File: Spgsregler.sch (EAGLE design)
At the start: 13 parts, among them X4 22-23-2031, X5 22-23-2031

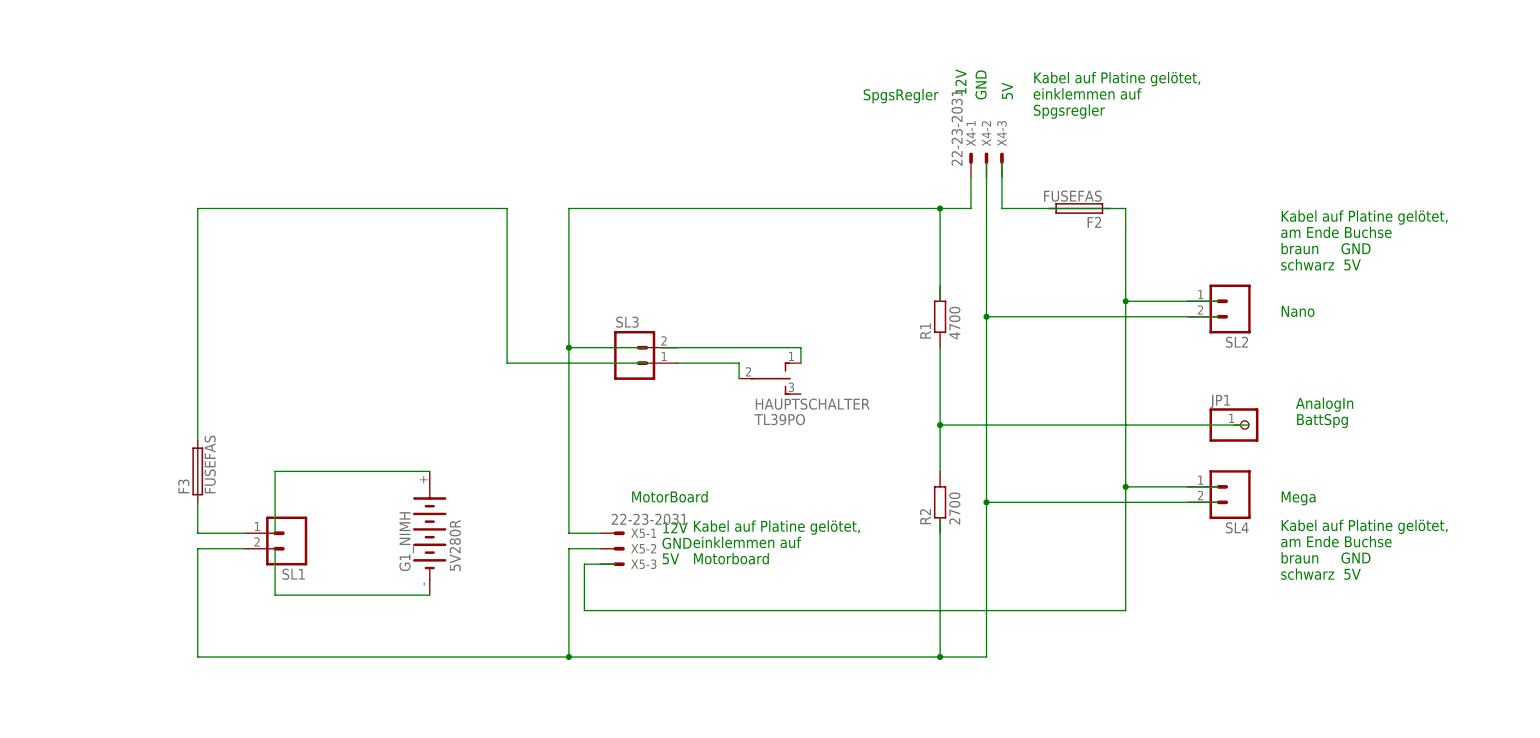
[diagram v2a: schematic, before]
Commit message: 
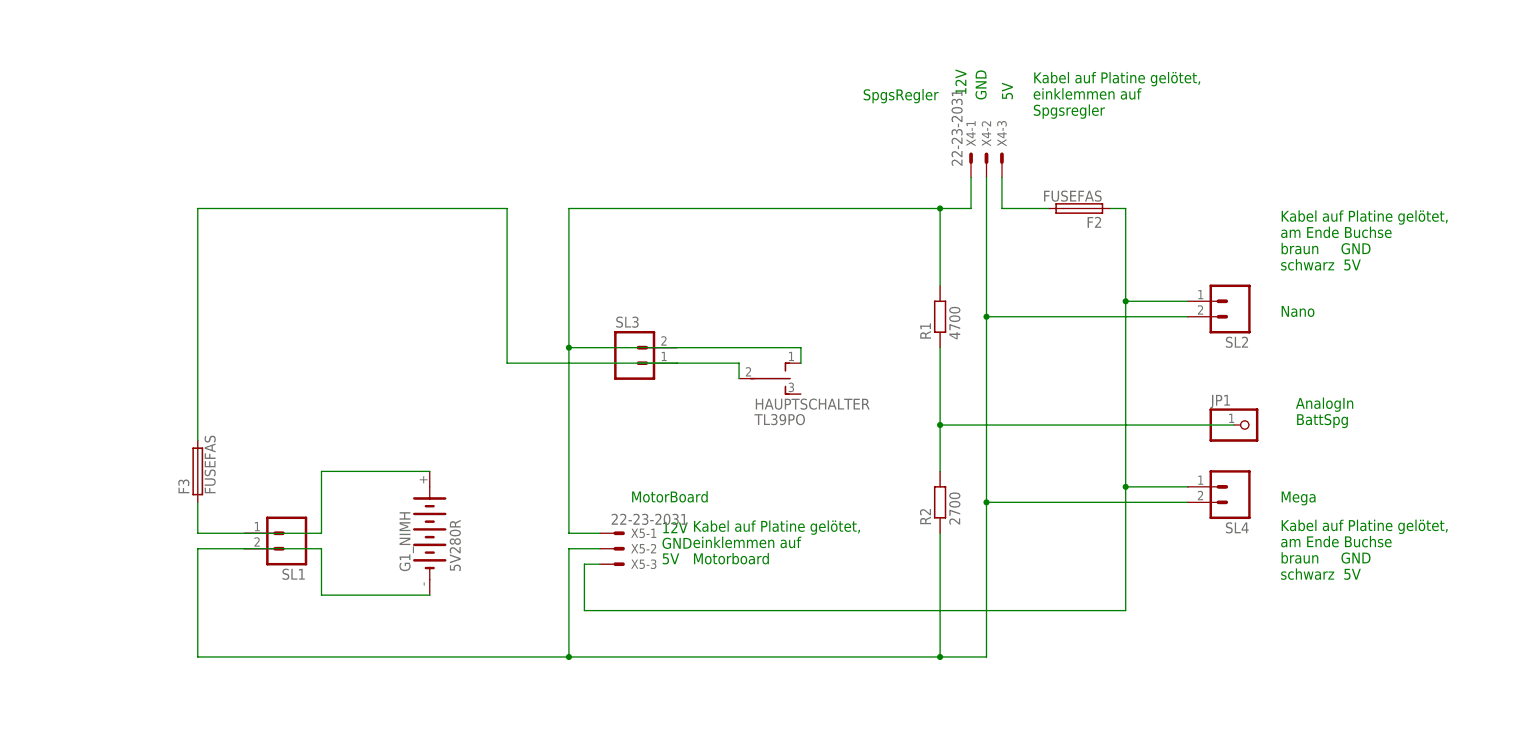
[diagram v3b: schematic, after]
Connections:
- removed net N$1: G1_NIMH.+
- removed net N$10: HAUPTSCHALTER.O
- removed net N$11: SL1.2, X5-2.S
- removed net N$9: HAUPTSCHALTER.P, SL3.1
- new net N$6: F2.2, X4-3.S
- net N$12: now also SL2.1, SL4.1, X5-3.S; no longer F2.2
- net N$2: now also R2.1, SL1.2, SL2.2, SL4.2, X4-2.S, X5-2.S
- net N$3: now also JP1.1
- net N$4: now also G1_NIMH.+; no longer SL1.1
- net N$5: now also HAUPTSCHALTER.O, R1.2
- net N$8: now also HAUPTSCHALTER.P, SL3.1
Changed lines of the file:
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@@
 <part name="X4" library="con-molex" deviceset="22-23-2031" device=""/>
 <part name="X5" library="con-molex" deviceset="22-23-2031" device=""/>
-<part name="FRAME1" library="frames" deviceset="A4L-LOC" device=""/>
+<part name="FRAME1" library="frames" deviceset="A4L-LOC" device="" value="WERTWERT"/>
 <part name="SL2" library="con-amp-quick" deviceset="M02" device=""/>
 <part name="SL4" library="con-amp-quick" deviceset="M02" device=""/>
@@
 </busses>
 <nets>
-<net name="N$1" class="0">
-<segment>
-<pinref part="G1_NIMH" gate="G$1" pin="+"/>
-<wire x1="43.18" y1="35.56" x2="17.78" y2="35.56" width="0.1524" layer="91"/>
-<wire x1="17.78" y1="35.56" x2="17.78" y2="25.4" width="0.1524" layer="91"/>
-</segment>
-</net>
-<net name="N$2" class="0">
-<segment>
-<wire x1="17.78" y1="22.86" x2="17.78" y2="15.24" width="0.1524" layer="91"/>
-<pinref part="G1_NIMH" gate="G$1" pin="-"/>
-<wire x1="17.78" y1="15.24" x2="43.18" y2="15.24" width="0.1524" layer="91"/>
-</segment>
-</net>
 <net name="N$8" class="0">
 <segment>
 <pinref part="F3" gate="G$1" pin="2"/>
-<wire x1="78.74" y1="53.34" x2="55.88" y2="53.34" width="0.1524" layer="91"/>
+<wire x1="83.82" y1="53.34" x2="55.88" y2="53.34" width="0.1524" layer="91"/>
 <wire x1="55.88" y1="78.74" x2="55.88" y2="53.34" width="0.1524" layer="91"/>
 <wire x1="5.08" y1="78.74" x2="55.88" y2="78.74" width="0.1524" layer="91"/>
 <wire x1="5.08" y1="40.64" x2="5.08" y2="78.74" width="0.1524" layer="91"/>
-</segment>
-</net>
-<net name="N$9" class="0">
-<segment>
 <pinref part="SL3" gate="G$1" pin="1"/>
 <pinref part="HAUPTSCHALTER" gate="BEF1" pin="P"/>
@@
 </segment>
 </net>
-<net name="N$10" class="0">
-<segment>
-<pinref part="HAUPTSCHALTER" gate="BEF1" pin="O"/>
-<wire x1="104.14" y1="53.34" x2="104.14" y2="55.88" width="0.1524" layer="91"/>
-<wire x1="104.14" y1="55.88" x2="81.28" y2="55.88" width="0.1524" layer="91"/>
-</segment>
-</net>
 <net name="N$12" class="0">
 <segment>
-<wire x1="144.78" y1="78.74" x2="154.94" y2="78.74" width="0.1524" layer="91"/>
-<pinref part="F2" gate="G$1" pin="2"/>
-<pinref part="F2" gate="G$1" pin="1"/>
-<wire x1="137.16" y1="86.36" x2="137.16" y2="78.74" width="0.1524" layer="91"/>
-<wire x1="137.16" y1="78.74" x2="144.78" y2="78.74" width="0.1524" layer="91"/>
-<wire x1="154.94" y1="78.74" x2="157.48" y2="78.74" width="0.1524" layer="91"/>
 <wire x1="157.48" y1="78.74" x2="157.48" y2="63.5" width="0.1524" layer="91"/>
 <wire x1="157.48" y1="63.5" x2="157.48" y2="33.02" width="0.1524" layer="91"/>
@@
 <wire x1="157.48" y1="12.7" x2="68.58" y2="12.7" width="0.1524" layer="91"/>
 <wire x1="68.58" y1="12.7" x2="68.58" y2="20.32" width="0.1524" layer="91"/>
-<wire x1="68.58" y1="20.32" x2="73.66" y2="20.32" width="0.1524" layer="91"/>
-<wire x1="172.72" y1="63.5" x2="157.48" y2="63.5" width="0.1524" layer="91"/>
-<wire x1="172.72" y1="33.02" x2="157.48" y2="33.02" width="0.1524" layer="91"/>
+<pinref part="F2" gate="G$1" pin="1"/>
+<wire x1="154.94" y1="78.74" x2="157.48" y2="78.74" width="0.1524" layer="91"/>
+<pinref part="SL2" gate="G$1" pin="1"/>
+<wire x1="167.64" y1="63.5" x2="157.48" y2="63.5" width="0.1524" layer="91"/>
 <junction x="157.48" y="63.5"/>
+<pinref part="SL4" gate="G$1" pin="1"/>
+<wire x1="167.64" y1="33.02" x2="157.48" y2="33.02" width="0.1524" layer="91"/>
 <junction x="157.48" y="33.02"/>
+<pinref part="X5" gate="-3" pin="S"/>
+<wire x1="68.58" y1="20.32" x2="71.12" y2="20.32" width="0.1524" layer="91"/>
 </segment>
 </net>
 <net name="N$4" class="0">
 <segment>
-<pinref part="SL1" gate="G$1" pin="1"/>
-<wire x1="12.7" y1="25.4" x2="5.08" y2="25.4" width="0.1524" layer="91"/>
+<pinref part="G1_NIMH" gate="G$1" pin="+"/>
+<wire x1="43.18" y1="35.56" x2="25.4" y2="35.56" width="0.1524" layer="91"/>
+<wire x1="25.4" y1="35.56" x2="25.4" y2="25.4" width="0.1524" layer="91"/>
 <pinref part="F3" gate="G$1" pin="1"/>
 <wire x1="5.08" y1="30.48" x2="5.08" y2="25.4" width="0.1524" layer="91"/>
+<wire x1="25.4" y1="25.4" x2="5.08" y2="25.4" width="0.1524" layer="91"/>
 </segment>
 </net>
 <net name="N$5" class="0">
 <segment>
-<wire x1="78.74" y1="55.88" x2="66.04" y2="55.88" width="0.1524" layer="91"/>
 <wire x1="66.04" y1="55.88" x2="66.04" y2="78.74" width="0.1524" layer="91"/>
 <wire x1="66.04" y1="78.74" x2="127" y2="78.74" width="0.1524" layer="91"/>
@@
 <pinref part="X4" gate="-1" pin="S"/>
 <wire x1="132.08" y1="78.74" x2="132.08" y2="83.82" width="0.1524" layer="91"/>
-<wire x1="127" y1="63.5" x2="127" y2="78.74" width="0.1524" layer="91"/>
+<pinref part="HAUPTSCHALTER" gate="BEF1" pin="O"/>
+<wire x1="104.14" y1="53.34" x2="104.14" y2="55.88" width="0.1524" layer="91"/>
+<wire x1="104.14" y1="55.88" x2="66.04" y2="55.88" width="0.1524" layer="91"/>
+<pinref part="R1" gate="G$1" pin="2"/>
+<wire x1="127" y1="66.04" x2="127" y2="78.74" width="0.1524" layer="91"/>
 <junction x="127" y="78.74"/>
-</segment>
-</net>
-<net name="N$11" class="0">
-<segment>
-<wire x1="134.62" y1="86.36" x2="134.62" y2="60.96" width="0.1524" layer="91"/>
-<wire x1="172.72" y1="60.96" x2="134.62" y2="60.96" width="0.1524" layer="91"/>
-<pinref part="SL1" gate="G$1" pin="2"/>
-<wire x1="12.7" y1="22.86" x2="5.08" y2="22.86" width="0.1524" layer="91"/>
-<wire x1="5.08" y1="5.08" x2="66.04" y2="5.08" width="0.1524" layer="91"/>
-<wire x1="71.12" y1="22.86" x2="66.04" y2="22.86" width="0.1524" layer="91"/>
-<wire x1="66.04" y1="22.86" x2="66.04" y2="5.08" width="0.1524" layer="91"/>
-<junction x="66.04" y="5.08"/>
-<wire x1="134.62" y1="5.08" x2="127" y2="5.08" width="0.1524" layer="91"/>
-<pinref part="X5" gate="-2" pin="S"/>
-<wire x1="134.62" y1="30.48" x2="134.62" y2="5.08" width="0.1524" layer="91"/>
-<wire x1="172.72" y1="30.48" x2="134.62" y2="30.48" width="0.1524" layer="91"/>
-<wire x1="5.08" y1="22.86" x2="5.08" y2="5.08" width="0.1524" layer="91"/>
-<wire x1="127" y1="5.08" x2="66.04" y2="5.08" width="0.1524" layer="91"/>
-<wire x1="134.62" y1="60.96" x2="134.62" y2="30.48" width="0.1524" layer="91"/>
-<junction x="127" y="5.08"/>
-<junction x="134.62" y="30.48"/>
-<junction x="134.62" y="60.96"/>
-<wire x1="127" y1="5.08" x2="127" y2="27.94" width="0.1524" layer="91"/>
 </segment>
 </net>
@@
 <pinref part="R1" gate="G$1" pin="1"/>
 <wire x1="127" y1="35.56" x2="127" y2="43.18" width="0.1524" layer="91"/>
+<pinref part="JP1" gate="G$1" pin="1"/>
 <wire x1="127" y1="43.18" x2="127" y2="55.88" width="0.1524" layer="91"/>
-<wire x1="177.8" y1="43.18" x2="127" y2="43.18" width="0.1524" layer="91"/>
+<wire x1="175.26" y1="43.18" x2="127" y2="43.18" width="0.1524" layer="91"/>
 <junction x="127" y="43.18"/>
+</segment>
+</net>
+<net name="N$6" class="0">
+<segment>
+<pinref part="F2" gate="G$1" pin="2"/>
+<wire x1="137.16" y1="78.74" x2="144.78" y2="78.74" width="0.1524" layer="91"/>
+<pinref part="X4" gate="-3" pin="S"/>
+<wire x1="137.16" y1="78.74" x2="137.16" y2="83.82" width="0.1524" layer="91"/>
+</segment>
+</net>
+<net name="N$2" class="0">
+<segment>
+<pinref part="G1_NIMH" gate="G$1" pin="-"/>
+<wire x1="25.4" y1="15.24" x2="43.18" y2="15.24" width="0.1524" layer="91"/>
+<wire x1="25.4" y1="15.24" x2="25.4" y2="22.86" width="0.1524" layer="91"/>
+<pinref part="SL1" gate="G$1" pin="2"/>
+<wire x1="12.7" y1="22.86" x2="5.08" y2="22.86" width="0.1524" layer="91"/>
+<wire x1="5.08" y1="5.08" x2="66.04" y2="5.08" width="0.1524" layer="91"/>
+<wire x1="71.12" y1="22.86" x2="66.04" y2="22.86" width="0.1524" layer="91"/>
+<wire x1="66.04" y1="22.86" x2="66.04" y2="5.08" width="0.1524" layer="91"/>
+<junction x="66.04" y="5.08"/>
+<pinref part="X5" gate="-2" pin="S"/>
+<wire x1="5.08" y1="22.86" x2="5.08" y2="5.08" width="0.1524" layer="91"/>
+<wire x1="134.62" y1="5.08" x2="127" y2="5.08" width="0.1524" layer="91"/>
+<wire x1="127" y1="5.08" x2="66.04" y2="5.08" width="0.1524" layer="91"/>
+<wire x1="134.62" y1="83.82" x2="134.62" y2="60.96" width="0.1524" layer="91"/>
+<wire x1="134.62" y1="60.96" x2="134.62" y2="30.48" width="0.1524" layer="91"/>
+<wire x1="134.62" y1="30.48" x2="134.62" y2="5.08" width="0.1524" layer="91"/>
+<pinref part="X4" gate="-2" pin="S"/>
+<pinref part="SL2" gate="G$1" pin="2"/>
+<wire x1="167.64" y1="60.96" x2="134.62" y2="60.96" width="0.1524" layer="91"/>
+<junction x="134.62" y="60.96"/>
+<pinref part="SL4" gate="G$1" pin="2"/>
+<wire x1="167.64" y1="30.48" x2="134.62" y2="30.48" width="0.1524" layer="91"/>
+<junction x="134.62" y="30.48"/>
+<pinref part="R2" gate="G$1" pin="1"/>
+<wire x1="127" y1="25.4" x2="127" y2="5.08" width="0.1524" layer="91"/>
+<junction x="127" y="5.08"/>
+<wire x1="25.4" y1="22.86" x2="12.7" y2="22.86" width="0.1524" layer="91"/>
 </segment>
 </net>
@@
 </sheet>
 </sheets>
+<errors>
+</errors>
 </schematic>
 </drawing>
